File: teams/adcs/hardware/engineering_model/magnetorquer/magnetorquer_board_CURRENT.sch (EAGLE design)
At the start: 40 parts

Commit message: ADCS/MT: Relabel component values and tidy up schematic
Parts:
- C12, C13, C14, C19, C20, C21, C6: device rcl:C-USC0805 -> DubSat1 Components:CAPACITOR0805
- C7, C8, C9: device rcl:C-EUC0805 -> DubSat1 Components:CAPACITOR0805
- R7: value (none) -> 330
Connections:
- net 6V renamed V_TORQ
- net N$10 renamed MT_X_B
- net N$11 renamed MT_X_A
- net N$12 renamed MT_Y_A
- net N$13 renamed MT_Y_B
- net N$14 renamed MT_Z_B
- net N$15 renamed MT_Z_A
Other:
- moved on the sheet: C12, C13, C14, C19, C20, C21, C6, C7, C8, C9, R1, R2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

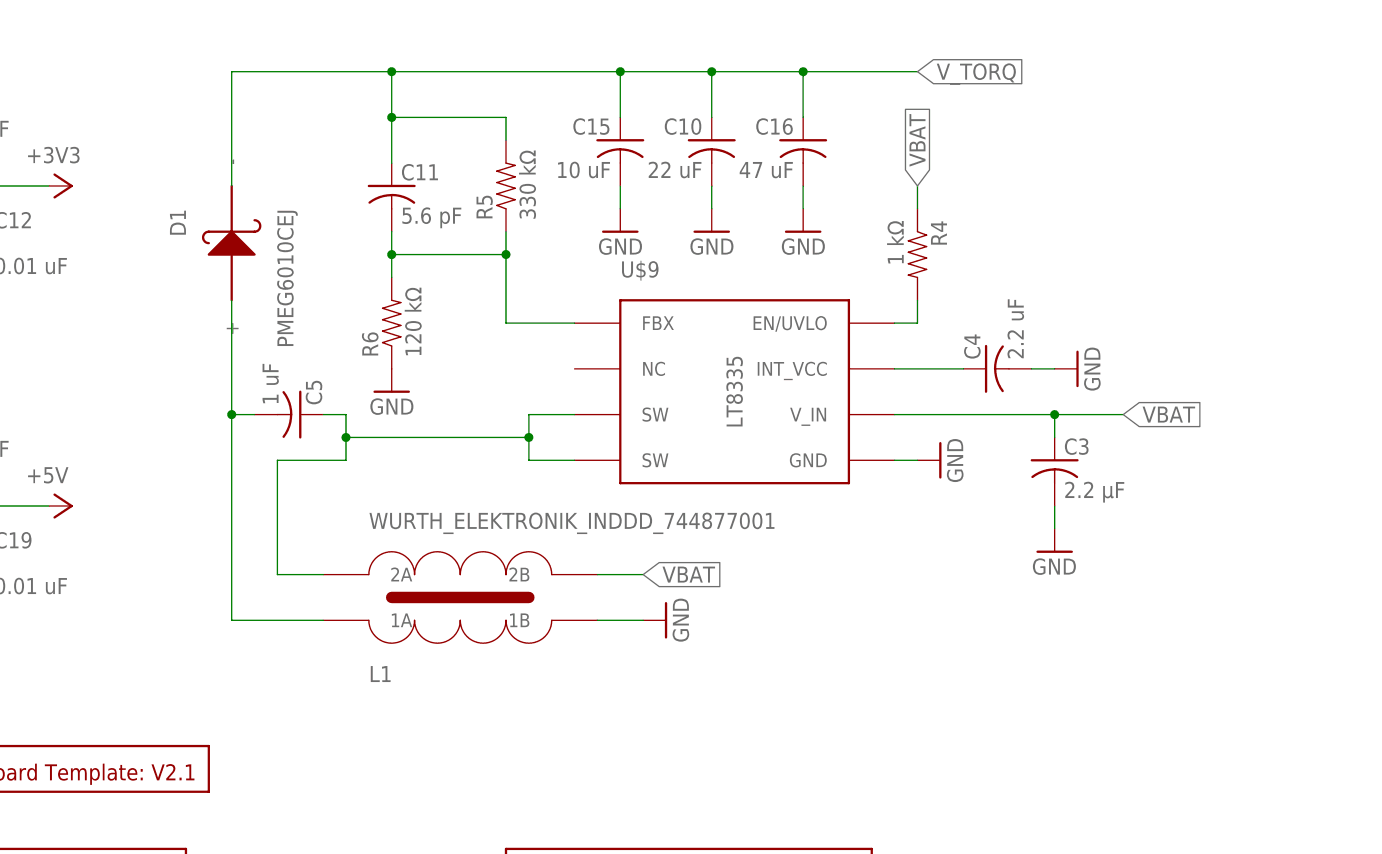
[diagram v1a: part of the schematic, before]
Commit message: ADCS/MT: Remove SEPIC converter
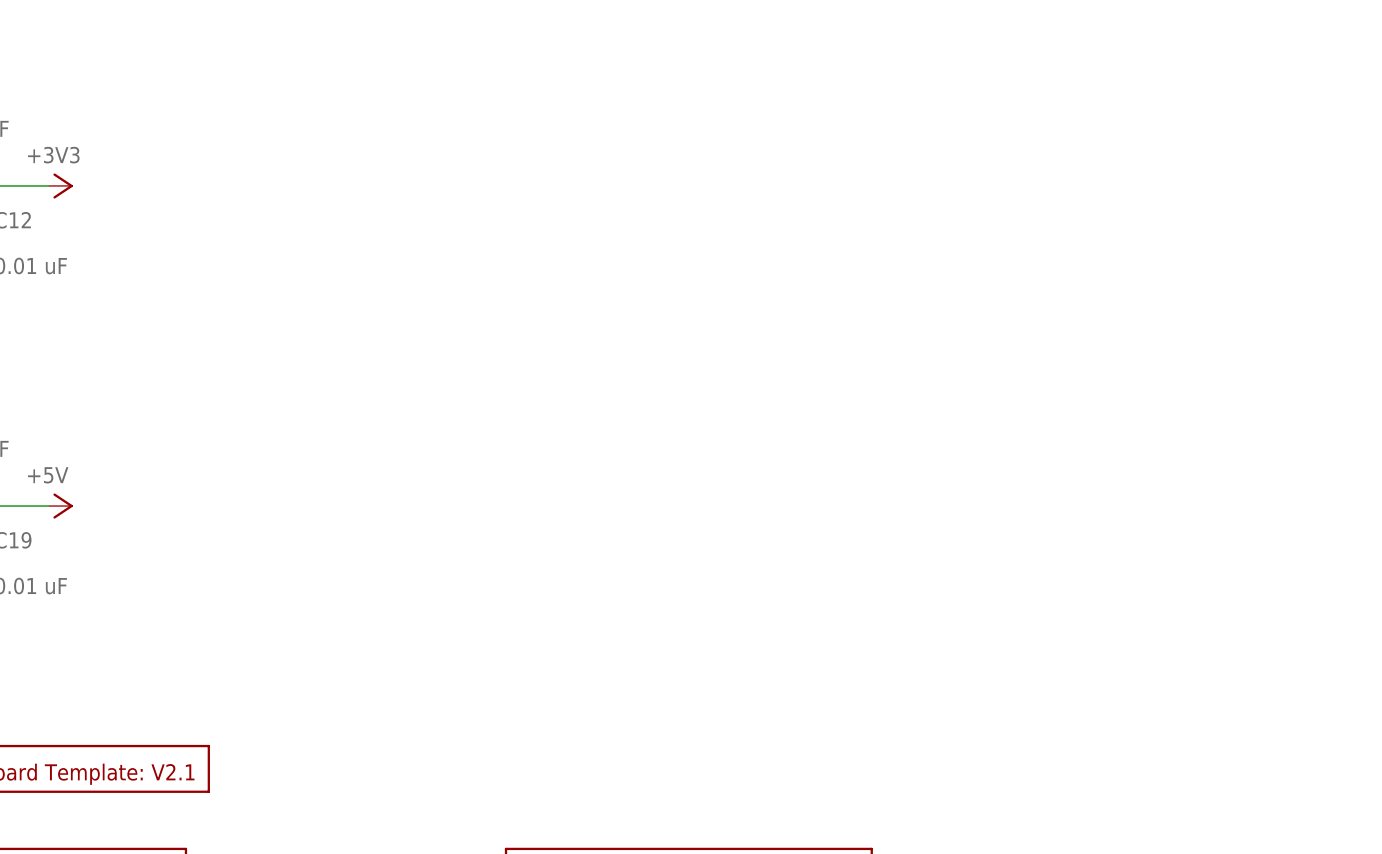
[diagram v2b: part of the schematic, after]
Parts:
- removed C10: 22 uF, rcl:C-USC1206
- removed C11: 5.6 pF, rcl:C-USC0805
- removed C15: 10 uF, rcl:C-USC0805
- removed C16: 47 uF, rcl:C-USC1206
- removed C3: 2.2 μF, rcl:C-USC0805
- removed C4: 2.2 uF, rcl:C-USC0805
- removed C5: 1 uF, rcl:C-USC0805
- removed D1: PMEG6010CEJ, DubSat1 Components:PMEG6010CEJ
- removed L1: WURTH_ELEKTRONIK_INDDD_744877001, DubSat1 Components:WURTH_ELEKTRONIK_INDDD_744877001
- removed R4: 1 kΩ, DubSat1 Components:RESISTOR0805
- removed R5: 330 kΩ, DubSat1 Components:RESISTOR0805
- removed R6: 120 kΩ, DubSat1 Components:RESISTOR0805
- removed U$9: LT8335, DubSat1 Components:LT8335
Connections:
- removed net EN_UVLO1: R4.2, U$9.EN/UVLO
- removed net FBX: C11.2, R5.1, R6.2, U$9.FBX
- removed net INT_VCC: C4.1, U$9.INT_VCC
- removed net SW: C5.1, L1.2A, U$9.SW@1, U$9.SW@2
- removed net VD: C5.2, D1.+, L1.1A
- net GND: no longer C10.2, C15.2, C16.2, C3.2, C4.2, L1.1B, R6.1, U$9.GND
- net VBAT: no longer C3.1, L1.2B, R4.1, U$9.V_IN
- net V_TORQ: no longer C10.1, C11.1, C15.1, C16.1, D1.-, R5.2
